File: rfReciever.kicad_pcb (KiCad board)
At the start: 4 copper layers, 33.8 x 20.5 mm, 38 parts, among them J1 MOLEX 1054440001, SW1 RF_RESET, SW2 RF_SLEEP, U1 CP2102N-A02-GQFN24, U2 USBLC6-2SC6, X1 DigiXBeeRX900Micro

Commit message: fixed traces and errors
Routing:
- net GND: track 0.00 -> 4.19 mm
- removed copper zone on B.Cu, net +5V
- removed copper zone on F.Cu, net +5V
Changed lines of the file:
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@@
 		(layer "Edge.Cuts")
+	)
+	(segment
+		(start 126.29125 67.95875)
+		(end 126 68.25)
+		(width 0.15)
+		(layer "F.Cu")
+		(net 1)
+	)
+	(segment
+		(start 126.45875 73.45875)
+		(end 126.25 73.25)
+		(width 0.15)
+		(layer "F.Cu")
+		(net 1)
+	)
+	(segment
+		(start 127.5 73.45875)
+		(end 126.45875 73.45875)
+		(width 0.15)
+		(layer "F.Cu")
+		(net 1)
+	)
+	(segment
+		(start 127.5 67.95875)
+		(end 126.29125 67.95875)
+		(width 0.15)
+		(layer "F.Cu")
+		(net 1)
+	)
+	(segment
+		(start 126.66 67.59)
+		(end 126 68.25)
+		(width 0.15)
+		(layer "F.Cu")
+		(net 1)
+	)
+	(segment
+		(start 126.66 67.28875)
+		(end 126.66 67.59)
+		(width 0.15)
+		(layer "F.Cu")
+		(net 1)
 	)
 	(via
@@
 	)
 	(segment
-		(start 124.25 71.81)
-		(end 124.69 71.81)
-		(width 0.36)
+		(start 127.5 70.95875)
+		(end 125.54125 70.95875)
+		(width 0.15)
 		(layer "F.Cu")
 		(net 43)
 	)
 	(segment
-		(start 124.69 71.81)
-		(end 125.5 71)
-		(width 0.36)
+		(start 124.9 71.6)
+		(end 119.9 71.6)
+		(width 0.15)
 		(layer "F.Cu")
 		(net 43)
 	)
 	(segment
-		(start 120.415 71.81)
-		(end 124.25 71.81)
-		(width 0.36)
+		(start 125.54125 70.95875)
+		(end 124.9 71.6)
+		(width 0.15)
 		(layer "F.Cu")
 		(net 43)
 	)
 	(segment
-		(start 127.5 71)
-		(end 125.5 71)
-		(width 0.3)
+		(start 119.9 71.6)
+		(end 119.75 71.75)
+		(width 0.15)
 		(layer "F.Cu")
 		(net 43)
 	)
 	(segment
-		(start 119.75 72.475)
-		(end 120.415 71.81)
-		(width 0.36)
+		(start 119.75 71.75)
+		(end 119.75 72.475)
+		(width 0.15)
 		(layer "F.Cu")
 		(net 43)
 	)
 	(segment
-		(start 124.45804 71.25)
-		(end 125.26804 70.44)
-		(width 0.36)
+		(start 125.54125 70.45875)
+		(end 124.75 71.25)
+		(width 0.15)
 		(layer "F.Cu")
 		(net 44)
 	)
 	(segment
-		(start 125.79196 70.5)
-		(end 125.73196 70.44)
-		(width 0.3)
+		(start 124.75 71.25)
+		(end 118.412501 71.25)
+		(width 0.15)
 		(layer "F.Cu")
 		(net 44)
 	)
 	(segment
-		(start 127.5 70.5)
-		(end 125.79196 70.5)
-		(width 0.3)
+		(start 118.412501 71.25)
+		(end 117.85 71.812501)
+		(width 0.15)
 		(layer "F.Cu")
 		(net 44)
 	)
 	(segment
-		(start 118.412501 71.25)
-		(end 124.45804 71.25)
-		(width 0.36)
+		(start 117.85 71.812501)
+		(end 117.85 72.475)
+		(width 0.15)
 		(layer "F.Cu")
 		(net 44)
 	)
 	(segment
-		(start 117.85 72.475)
-		(end 117.85 71.812501)
-		(width 0.36)
-		(layer "F.Cu")
-		(net 44)
-	)
-	(segment
-		(start 125.26804 70.44)
-		(end 125.73196 70.44)
-		(width 0.36)
-		(layer "F.Cu")
-		(net 44)
-	)
-	(segment
-		(start 117.85 71.812501)
-		(end 118.412501 71.25)
-		(width 0.36)
+		(start 127.5 70.45875)
+		(end 125.54125 70.45875)
+		(width 0.15)
 		(layer "F.Cu")
 		(net 44)
@@
 	)
 	(segment
-		(start 117.270957 74.170957)
-		(end 117.85 74.75)
-		(width 0.15)
-		(layer "F.Cu")
-		(net 46)
-	)
-	(segment
-		(start 117.270957 73.773749)
-		(end 117.270957 74.170957)
+		(start 117.85 73.95375)
+		(end 117.75 73.85375)
 		(width 0.15)
 		(layer "F.Cu")
@@
 	)
 	(segment
+		(start 117.75 73.85375)
+		(end 117.356264 73.85375)
+		(width 0.15)
+		(layer "F.Cu")
+		(net 46)
+	)
+	(segment
 		(start 115.673751 73.28875)
 		(end 116.785958 73.28875)
@@
 	)
 	(segment
+		(start 117.85 74.75)
+		(end 117.85 73.95375)
+		(width 0.15)
+		(layer "F.Cu")
+		(net 46)
+	)
+	(segment
 		(start 115.602501 73.36)
 		(end 115.673751 73.28875)
@@
 	)
 	(segment
+		(start 117.276263 73.773749)
+		(end 117.270957 73.773749)
+		(width 0.15)
+		(layer "F.Cu")
+		(net 46)
+	)
+	(segment
+		(start 117.356264 73.85375)
+		(end 117.276263 73.773749)
+		(width 0.15)
+		(layer "F.Cu")
+		(net 46)
+	)
+	(segment
 		(start 119.162499 73.5)
 		(end 119.75 74.087501)
@@
 	)
 	(zone
-		(net 36)
-		(net_name "+5V")
-		(layers "F&B.Cu")
-		(hatch edge 0.5)
-		(priority 1)
-		(connect_pads
-			(clearance 0.5)
-		)
-		(min_thickness 0.25)
-		(filled_areas_thickness no)
-		(fill yes
-			(thermal_gap 0.5)
-			(thermal_bridge_width 0.5)
-		)
-		(polygon
-			(pts
-				(xy 94.75 60.5) (xy 128.5 60.5) (xy 128.5 81) (xy 94.75 81)
-			)
-		)
-	)
-	(zone

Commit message: reworked schematic v1 matthew review
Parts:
- removed U1: CP2102N-A02-GQFN24, rfReciever-Footprints:QFN50P500X500X80-29N
- added C10: 1uF, Capacitor_SMD:C_0805_2012Metric, F.Cu at (129.4, 91.8)
- added C11: 4.7uF, Capacitor_SMD:C_0805_2012Metric, F.Cu at (129.4, 94.8)
- added C12: 0.1uF, Capacitor_SMD:C_0805_2012Metric, F.Cu at (129.4, 97.8)
- added R14: 27, Resistor_SMD:R_0805_2012Metric, F.Cu at (133.8, 91.8)
- added R19: 27, Resistor_SMD:R_0805_2012Metric, F.Cu at (133.8, 94.8)
- added U3: FT234XD-R, rfReciever-Footprints:SON45P300X300X80-13N, F.Cu at (107.6, 88.5)
- added U4: TPS76333DBVT, rfReciever-Footprints:SOT95P280X145-5N, F.Cu at (107.5, 93.0)
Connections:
- J1 pad A4: /MLX(VBUS) -> +5V
- J1 pad A9: /MLX(VBUS) -> +5V
- J1 pad B4: /MLX(VBUS) -> +5V
- J1 pad B9: /MLX(VBUS) -> +5V
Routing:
- net +3.3V: track 48.4 -> 0.00 mm, vias 2 -> 0
- net /RF_BOOTMODE: track 27.5 -> 0.00 mm, vias 3 -> 0
- net /RF_PWM: track 19.7 -> 0.00 mm, vias 1 -> 0
- net /MLX(VBUS): track 13.5 -> 0.00 mm
- net /UART_CTS: track 13.4 -> 0.00 mm, vias 1 -> 0
- net /RF_RESET: track 12.6 -> 0.00 mm, vias 1 -> 0
- net /RF_DSLEEP: track 12.1 -> 0.00 mm, vias 1 -> 0
- net /RF_RXD: track 11.8 -> 0.00 mm, vias 1 -> 0
- net +5V: track 11.3 -> 0.00 mm, vias 1 -> 0
- net /UART_RTS: track 11.2 -> 0.00 mm, vias 1 -> 0
- net /RF_TXD: track 11.0 -> 0.00 mm, vias 1 -> 0
- net /MLX(D+): track 10.9 -> 0.00 mm
- net /RF_ASSOCIATE: track 10.2 -> 0.00 mm, vias 1 -> 0
- net /MLX(D-): track 8.80 -> 0.00 mm
- net Net-(U1-~{RXT}/GPIO.3): track 8.43 -> 0.00 mm
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
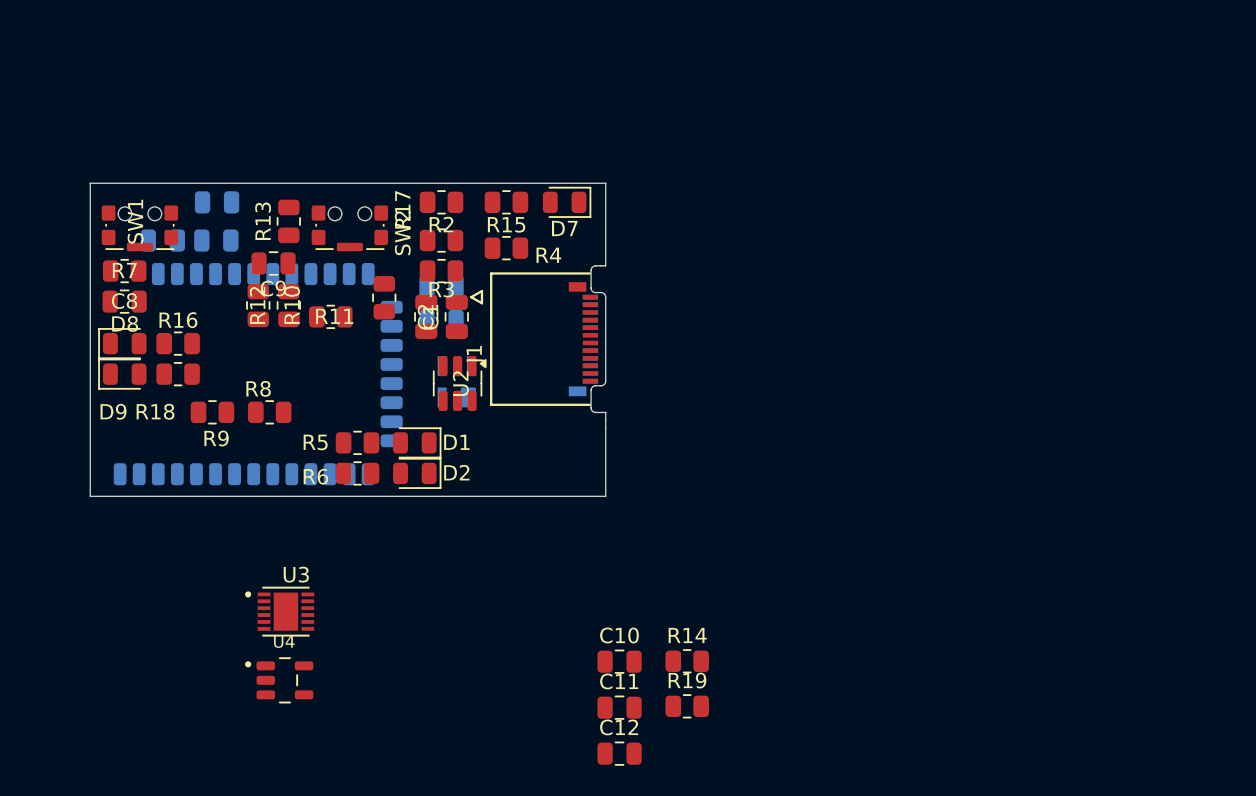
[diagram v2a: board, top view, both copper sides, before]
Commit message: schematic mk2 post matthew review
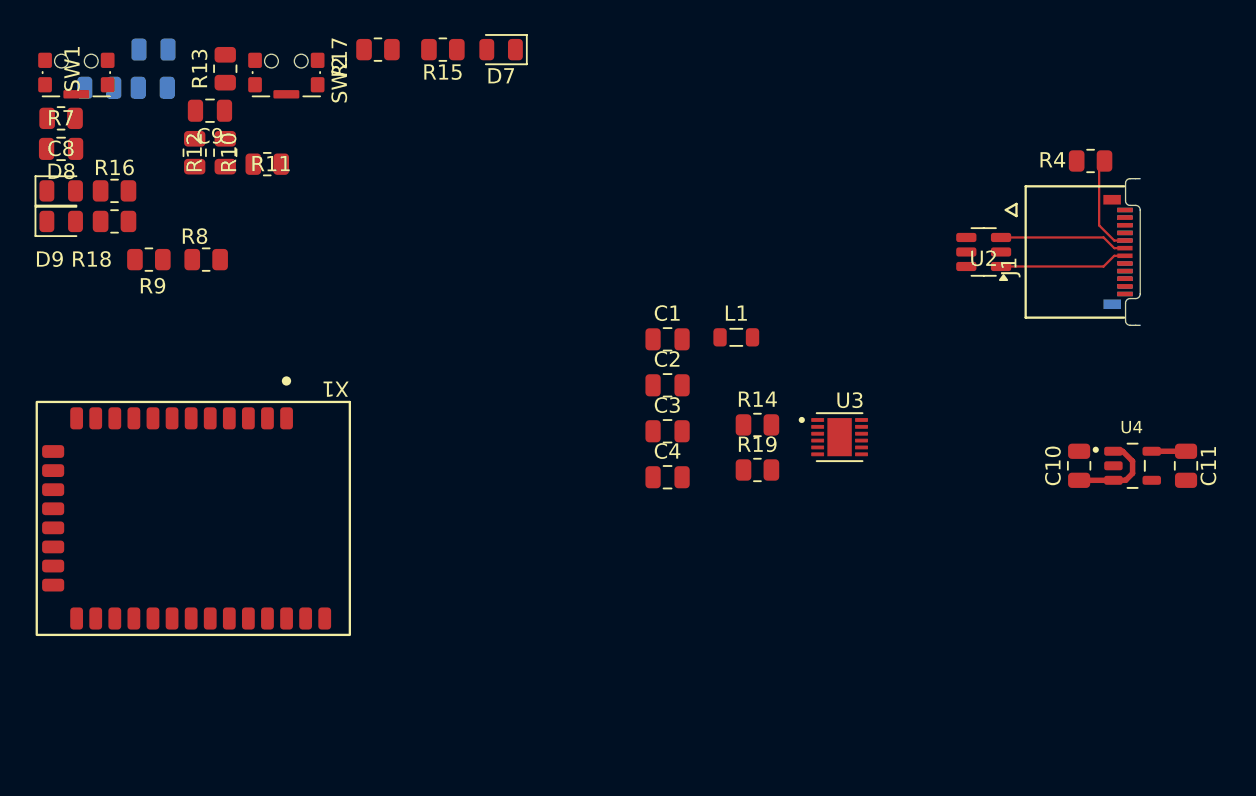
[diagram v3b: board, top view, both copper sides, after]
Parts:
- removed C12: 0.1uF, Capacitor_SMD:C_0805_2012Metric
- removed D1, D2: LED, LED_SMD:LED_0805_2012Metric
- removed D3: SP0503BAHTG, rfReciever-Footprints:SOT143
- removed R1, R5, R6: 1K, Resistor_SMD:R_0805_2012Metric
- removed R2: 47.5K, Resistor_SMD:R_0805_2012Metric
- removed R3: 22.1K, Resistor_SMD:R_0805_2012Metric
- added L1: 4.7 uH, Inductor_SMD:L_0805_2012Metric, F.Cu at (137.1, 70.6)
- C1: value 4.7uF -> 10nF
- C3: value 4.7uF -> 0.1uF; moved to F.Cu
- C4, X1: moved to F.Cu
- moved U4 57.3 mm to (163.0, 79.0)
- moved C11 40.3 mm to (166.5, 79.0), turned to -90 degrees
- moved R4 38.7 mm to (160.2, 59.0)
- moved U3 38.0 mm to (143.8, 77.1)
- moved U2 35.5 mm to (153.2, 65.0), turned to 180 degrees
- moved J1 35.5 mm to (163.5, 65.0)
- moved C10 32.7 mm to (159.5, 79.0), turned to 90 degrees
- moved C4 18.0 mm to (132.6, 79.8), turned to 0 degrees
- moved C3 17.6 mm to (132.6, 76.7), turned to 0 degrees
- moved C2 16.4 mm to (132.6, 73.7), turned to 0 degrees
- moved R14 16.1 mm to (138.4, 76.3)
- moved R19 16.1 mm to (138.4, 79.3)
- moved C1 13.9 mm to (132.6, 70.7), turned to 0 degrees
- moved C5 10.8 mm to (95.3, 54.2)
- moved C6 10.8 mm to (98.8, 54.2)
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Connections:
- C2 pad 1: +5V -> /FTDI_3.3V
- C3 pad 1: GND -> /FTDI_3.3V
- C3 pad 2: +3.3V -> GND
- C4 pad 1: GND -> /FTDI_VCC
- C4 pad 2: +3.3V -> GND
- U2 pad 5: GND -> +5V
- U3 pad 2: +3.3V -> /FTDI_3.3V
- U3 pad 3: +3.3V -> /FTDI_3.3V
- U3 pad 4: +3.3V -> /FTDI_VCC
- U3 pad 6: +3.3V -> /VCCIO
- U3 pad 9: +3.3V -> /FTDI_3.3V
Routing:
- net /MLX(D-): track 0.00 -> 8.40 mm
- net /MLX(D+): track 0.00 -> 8.40 mm
- net Net-(J1-CC): track 0.00 -> 6.46 mm
- net +5V: track 0.00 -> 6.01 mm
- net +3.3V: track 0.00 -> 2.25 mm
- removed copper zone on In1.Cu, net GND
- removed copper zone on In2.Cu, net GND
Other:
- board size 33.8 x 20.5 mm -> 1 x 9.6 mm

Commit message: gitignore + layout v3 + routing
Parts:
- C4, C8, C9, R10, R11, R13, R14, R17, R19, U3, X1: moved to B.Cu
- C5, C6, C7: moved to F.Cu
- moved SW1 61.8 mm to (146.3, 85.8), turned to 0 degrees
- moved C8 57.7 mm to (144.1, 84.8), turned to 0 degrees
- moved C5 56.8 mm to (147.6, 76.3)
- moved C7 56.5 mm to (147.6, 80.3), turned to 180 degrees
- moved SW2 54.9 mm to (151.8, 85.8), turned to 0 degrees
- moved C6 54.4 mm to (147.6, 78.3), turned to 180 degrees
- moved R7 53.7 mm to (142.1, 77.8), turned to 90 degrees
- moved D9 53.6 mm to (146.1, 69.3), turned to 180 degrees
- moved D8 50.4 mm to (142.6, 69.3), turned to 180 degrees
- moved R18 48.4 mm to (143.8, 72.3), turned to -90 degrees
- moved R12 48.0 mm to (144.6, 79.9), turned to -90 degrees
- moved R9 47.9 mm to (146.1, 72.1), turned to 90 degrees
- moved C9 47.7 mm to (140.6, 84.6), turned to 0 degrees
- moved R13 47.1 mm to (137.9, 85.3), turned to -90 degrees
- moved R16 46.6 mm to (141.6, 72.3), turned to -90 degrees
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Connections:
- net /MLX(D+) renamed /MLXDP
- net /MLX(D-) renamed /MLXDN
- net Net-(U3-USBDM) renamed /USBDM
- net Net-(U3-USBDP) renamed /USBDP
- U3 pad 6: /VCCIO -> /FTDI_3.3V
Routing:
- net +3.3V: track 2.25 -> 66.0 mm, vias 0 -> 3
- net /RF_TXD: track 0.00 -> 52.2 mm
- net /RF_RXD: track 0.00 -> 38.0 mm
- net /UART_CTS: track 0.00 -> 29.3 mm, vias 0 -> 2
- net +5V: track 6.01 -> 32.6 mm, vias 0 -> 1
- net /UART_RTS: track 0.00 -> 26.5 mm, vias 0 -> 1
- net /RF_SW_SLEEP: track 0.00 -> 17.6 mm, vias 0 -> 1
- net /FTDI_3.3V: track 0.00 -> 17.3 mm, vias 0 -> 3
- net /RF_SW_RESET: track 0.00 -> 15.1 mm
- net /RF_RESET: track 0.00 -> 7.92 mm, vias 0 -> 2
- net /RF_SLEEP: track 0.00 -> 7.87 mm
- net /RF_D8: track 0.00 -> 5.21 mm
- net /RF_D9: track 0.00 -> 5.09 mm
- net /RF_ASSOCIATE: track 0.00 -> 2.58 mm, vias 0 -> 1
- net /RF_BOOTMODE: track 0.00 -> 2.55 mm
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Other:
- board size 1 x 9.6 mm -> 24.8 x 34 mm

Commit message: revisions requested by Lakshay, new LDO
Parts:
- removed C1: 10nF, Capacitor_SMD:C_0805_2012Metric
- removed C3, C4: 0.1uF, Capacitor_SMD:C_0805_2012Metric
- removed L1: 4.7 uH, Inductor_SMD:L_0805_2012Metric
- removed U4: TPS76333DBVT, rfReciever-Footprints:SOT95P280X145-5N
- added C12: 47pF, Capacitor_SMD:C_0805_2012Metric, F.Cu at (141.4, 64.8)
- added C13: 47pF, Capacitor_SMD:C_0805_2012Metric, F.Cu at (141.4, 58.2)
- added U1: TLV70130DBVR, rfReciever-Footprints:DBV5, B.Cu at (144.2, 57.2)
- C11: value 4.7uF -> 1uF
- C2: value 0.1uF -> 100nF
- R14, R19: moved to F.Cu
- moved R11 7.29 mm to (135.2, 86.8), turned to 0 degrees
- moved C11 3.38 mm to (142.8, 56.0), turned to 0 degrees
- moved C2 1.97 mm to (137.7, 65.5)
- moved C10 1.49 mm to (145.8, 58.5), turned to 180 degrees
- moved R14 0.27 mm to (141.4, 62.8)
- moved R19 0.27 mm to (141.4, 60.2)
- moved U3 0.11 mm to (137.9, 61.5)
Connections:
- C2 pad 1: /FTDI_3.3V -> /FTDI_RESET
- U3 pad 2: /FTDI_3.3V -> /FTDI_RESET
- U3 pad 3: /FTDI_3.3V -> /FTDI_RESET
- U3 pad 4: /FTDI_VCC -> +3.3V
- U3 pad 6: /FTDI_3.3V -> unconnected-(U3-CBUS0-Pad6)
- U3 pad 9: /FTDI_3.3V -> /FTDI_RESET
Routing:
- net /FTDI_3.3V: track 17.3 -> 0.00 mm, vias 3 -> 0
- net /FTDI_RESET: track 0.00 -> 15.4 mm, vias 0 -> 2
- net +3.3V: track 66.0 -> 78.7 mm, vias 3 -> 6
- net +5V: track 32.6 -> 22.1 mm, vias 1 -> 2
- net /RF_RXD: track 38.0 -> 47.0 mm, vias 0 -> 2
- net /RF_TXD: track 52.2 -> 48.8 mm
- net /USB_OUT_D+: track 1.96 -> 4.16 mm
- net /USB_OUT_D-: track 2.00 -> 4.21 mm
- net /FTDI_VCC: track 1.49 -> 0.00 mm
- net /UART_RTS: track 26.5 -> 25.5 mm
- net /UART_CTS: track 29.3 -> 28.3 mm
- net /RF_D9: track 5.09 -> 4.46 mm
- net /USBDM: track 1.86 -> 1.51 mm, vias 0 -> 1
- net /USBDP: track 1.59 -> 1.61 mm, vias 0 -> 1
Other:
- board size 24.8 x 34 mm -> 22.8 x 34 mm

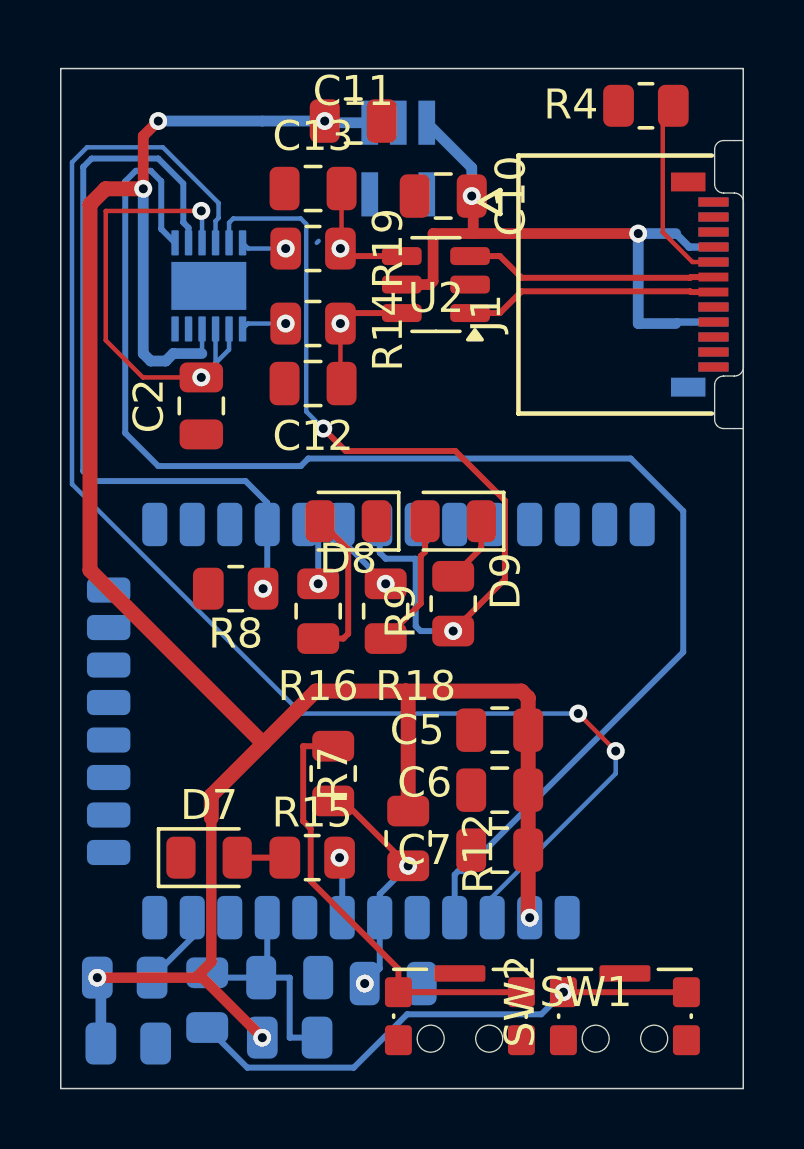
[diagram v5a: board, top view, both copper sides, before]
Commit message: reworked layout slightly + 3d models
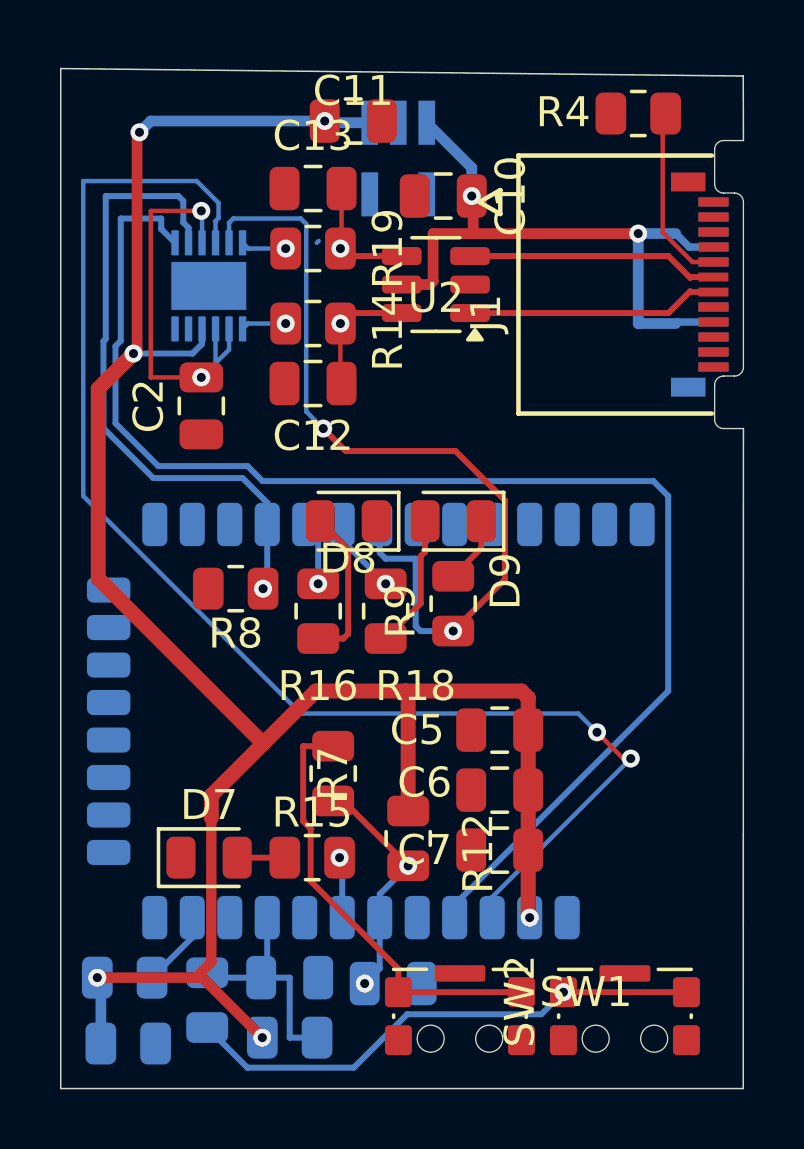
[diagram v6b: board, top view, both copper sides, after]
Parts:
- moved R4 0.36 mm to (152.2, 55.8)
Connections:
- net /MLXDN renamed /USBMLXDN
- net /MLXDP renamed /USBMLXDP
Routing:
- net +3.3V: track 78.7 -> 72.8 mm
- net /UART_RTS: track 25.5 -> 21.3 mm
- net /RF_TXD: track 48.8 -> 45.7 mm
- net /FTDI_RESET: track 15.4 -> 13.1 mm
- net /RF_RXD: track 47.0 -> 45.8 mm
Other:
- outline, holes or cut-outs redrawn
